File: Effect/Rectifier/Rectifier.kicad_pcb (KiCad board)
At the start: 2 copper layers, 32 x 68.5 mm, 33 parts, among them J1 Conn_01x04_Pin, J2 Conn_01x03_Pin, U1 OPA1656, U2 OPA1656

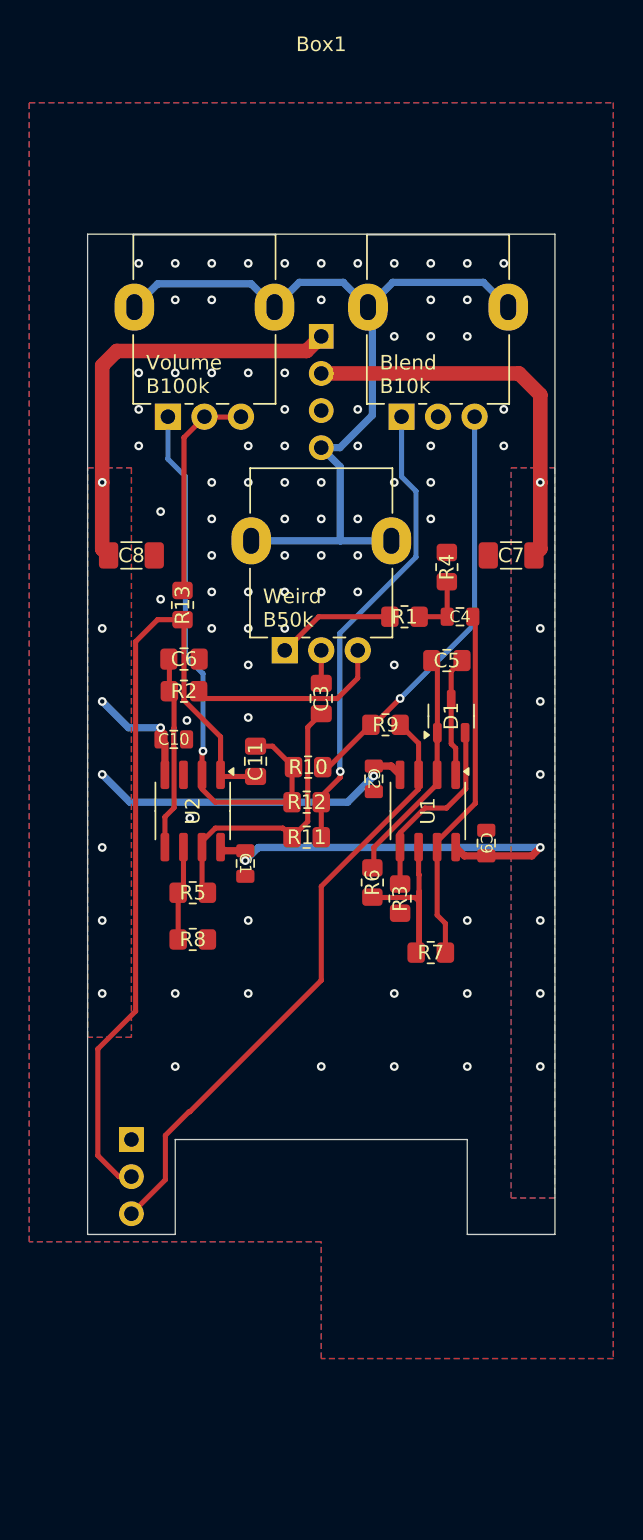
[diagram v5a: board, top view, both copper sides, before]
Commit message: Update all remaining effects boards to use global ground and GNDREF
Let's just make it the rule that we only call the actual external ground
GND, and don't play with local grounds.  That makes things like the
potentiometer shield pins so much simpler to deal with, and means that
ground pours are actual ground pours.

The GNDREF uses are fairly few in the end, and it's much better to make
them explicit.

Signed-off-by: Linus Torvalds <torvalds@linux-foundation.org>
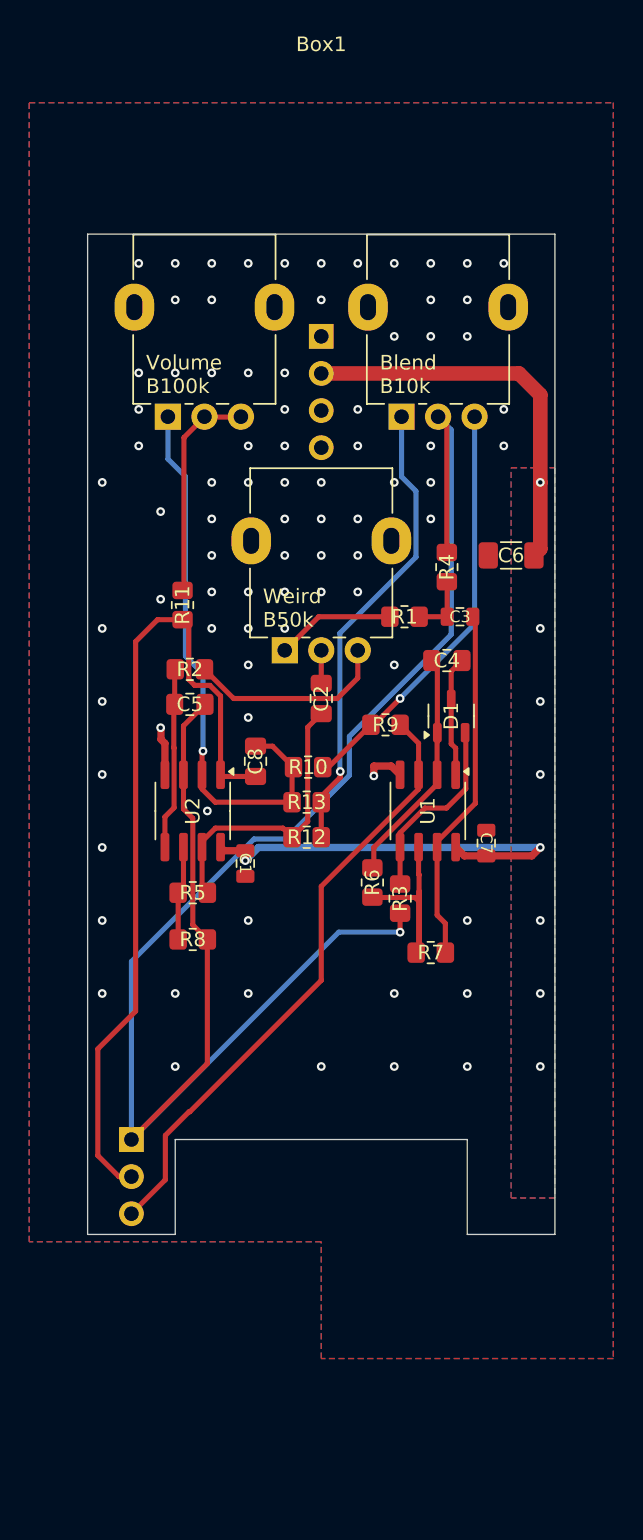
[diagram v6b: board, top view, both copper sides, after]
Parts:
- removed C10: 0.1uF, Mylib:C_0704_1810Metric
- removed the C2 at (103.6, 100.3)
- removed the C8 at (87.0, 85.0)
- moved C5 3.13 mm to (91.0, 95.2)
- moved R2 1.55 mm to (91.0, 92.8)
- renumbered C3 to C2, C4 to C3, C5 to C4, C6 to C5, C7 to C6, C9 to C7, C11 to C8, R13 to R11, R11 to R12, R12 to R13
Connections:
- C5 pad 2: GND -> GNDREF
- J1 pad 1: -V -> GND
- J1 pad 3: GND -> unconnected-(J1-Pin_3-Pad3)
- J1 pad 4: SHIELD -> GND
- J2 pad 1: GND -> GNDREF
- R3 pad 1: GND -> GNDREF
- R4 pad 1: GND -> GNDREF
- R8 pad 2: GND -> GNDREF
- RV1 pad MP: SHIELD -> GND
- RV2 pad 2: GND -> GNDREF
- RV2 pad MP: SHIELD -> GND
- RV3 pad MP: SHIELD -> GND
- U1 pad 4: -V -> GND
- U2 pad 3: GND -> GNDREF
- U2 pad 4: -V -> GND
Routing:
- net GNDREF: track 0.00 -> 128.6 mm, vias 0 -> 1
- net SHIELD: track 60.1 -> 0.00 mm
- net -V: track 60.0 -> 0.00 mm, vias 9 -> 0
- net GND: track 0.00 -> 6.07 mm, vias 74 -> 82
- removed copper zone on B.Cu, net -V
- removed copper zone on F.Cu, net -V

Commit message: Update rectifier board to the quad opamp
Intentionally fairly dense layout (for me) to see how it is to solder.
I'm sure it could be routed better, but it is what it is.

Signed-off-by: Linus Torvalds <torvalds@linux-foundation.org>
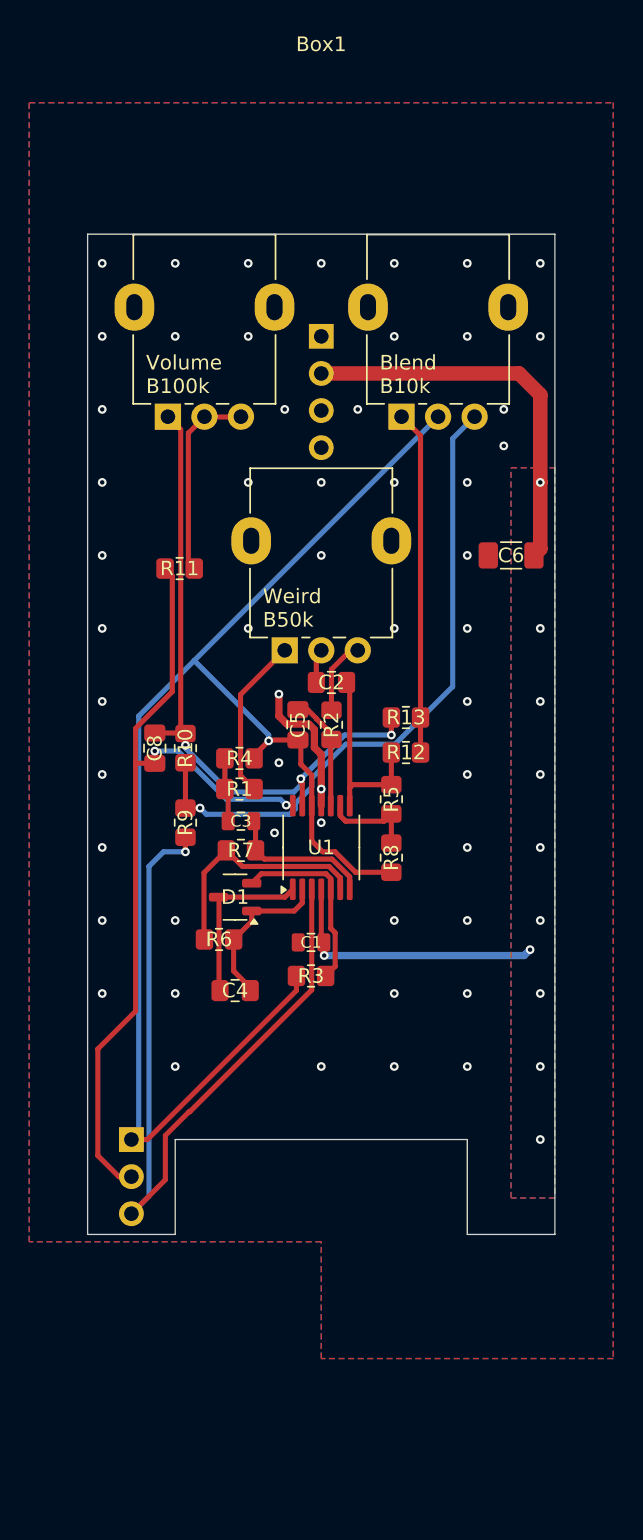
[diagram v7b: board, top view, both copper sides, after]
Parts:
- removed C7: 0.1uF, Mylib:C_0704_1810Metric
- removed U2: OPA1656, Package_SO:SOIC-8_3.9x4.9mm_P1.27mm
- U1: value OPA1656 -> OPA1664; footprint Package_SO:SOIC-8_3.9x4.9mm_P1.27mm -> Package_SO:TSSOP-14_4.4x5mm_P0.65mm
- moved C4 26.9 mm to (94.1, 114.8), turned to 180 degrees
- moved C3 20.5 mm to (94.5, 103.2)
- moved R4 19.3 mm to (94.4, 98.9), turned to 180 degrees
- moved D1 19.3 mm to (94.1, 108.4), turned to 180 degrees
- moved R1 16.3 mm to (94.4, 101.0), turned to 0 degrees
- moved R9 15.3 mm to (90.7, 103.3), turned to -90 degrees
- moved R5 15.0 mm to (104.8, 101.7), turned to -90 degrees
- moved R7 14.8 mm to (94.5, 105.2)
- moved R8 14.7 mm to (104.8, 105.7), turned to -90 degrees
- moved R6 11.2 mm to (93.0, 111.3), turned to 180 degrees
- moved R2 10.4 mm to (100.7, 96.6), turned to -90 degrees
- moved R13 8.94 mm to (105.8, 96.1)
- moved R12 8.94 mm to (105.8, 98.5)
- moved R10 8.50 mm to (90.7, 98.2), turned to -90 degrees
- moved R3 8.08 mm to (99.3, 113.8), turned to 0 degrees
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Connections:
- C5 pad 1: Net-(U2B-+) -> Net-(U1C-+)
- C8 pad 2: Net-(U2A--) -> Net-(U1D--)
- R10 pad 1: Net-(U2A--) -> Net-(U1D--)
- R13 pad 1: Net-(U2A--) -> Net-(U1D--)
- R2 pad 2: Net-(U2B-+) -> Net-(U1C-+)
- R5 pad 2: Net-(U2B--) -> Net-(U1C--)
- R8 pad 1: Net-(U2B--) -> Net-(U1C--)
- RV3 pad 1: Net-(U2A--) -> Net-(U1D--)
- U1 pad 4: GND -> +V
- U1 pad 8: +V -> FILTERED
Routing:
- net Net-(U1D--): track 0.00 -> 45.1 mm, vias 0 -> 3
- net Net-(U2A--): track 38.5 -> 0.00 mm, vias 1 -> 0
- net GNDREF: track 128.6 -> 98.4 mm
- net Net-(R10-Pad2): track 28.0 -> 44.9 mm
- net RECT: track 23.8 -> 9.93 mm
- net IN: track 42.2 -> 55.6 mm, vias 0 -> 1
- net Net-(U2B-+): track 12.5 -> 0.00 mm
- net +V: track 56.1 -> 45.4 mm, vias 9 -> 11
- net Net-(R2-Pad1): track 13.8 -> 4.64 mm
- net Net-(R12-Pad1): track 31.5 -> 23.5 mm, vias 1 -> 0
- net Net-(U1C-+): track 0.00 -> 7.85 mm
- net Net-(U1C--): track 0.00 -> 6.55 mm
- net Net-(U2B--): track 5.96 -> 0.00 mm
- net FILTERED: track 18.9 -> 13.4 mm
- net Net-(D1A-A): track 14.9 -> 10.9 mm
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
